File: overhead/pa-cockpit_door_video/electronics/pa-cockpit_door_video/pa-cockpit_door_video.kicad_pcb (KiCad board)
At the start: 2 copper layers, 145 x 47.3 mm, 30 parts, among them J1 Conn_02x01, J3 Conn_02x03_Counter_Clockwise

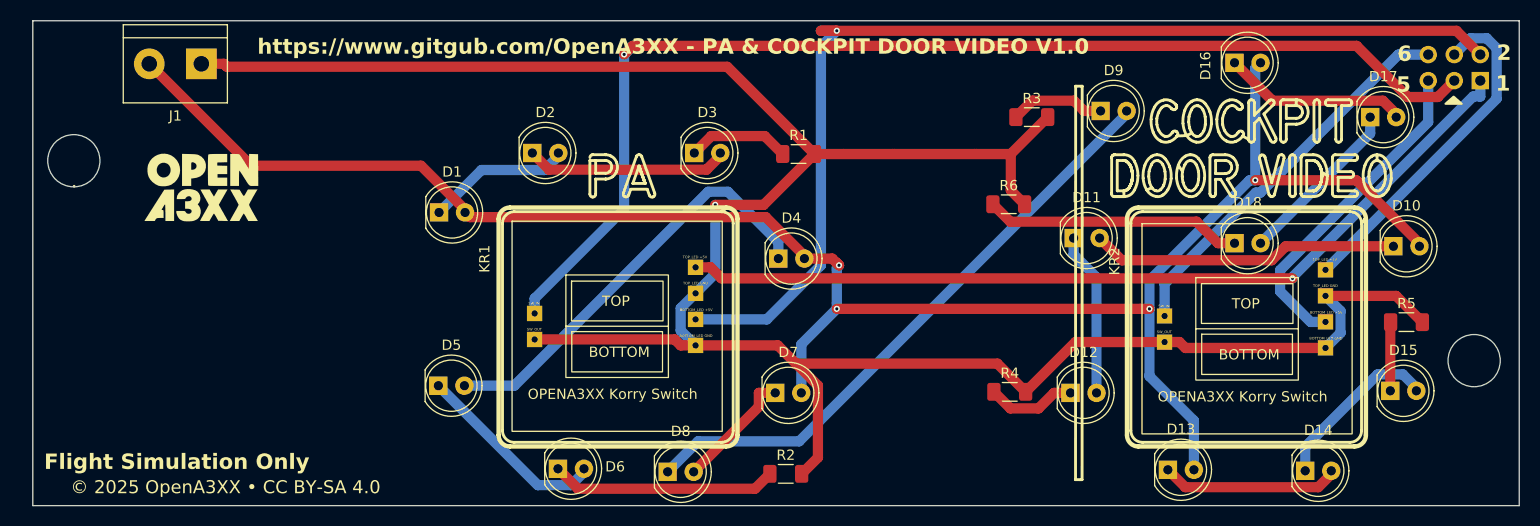
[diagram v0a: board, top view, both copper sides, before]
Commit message: Updated all LEDs for SMD!
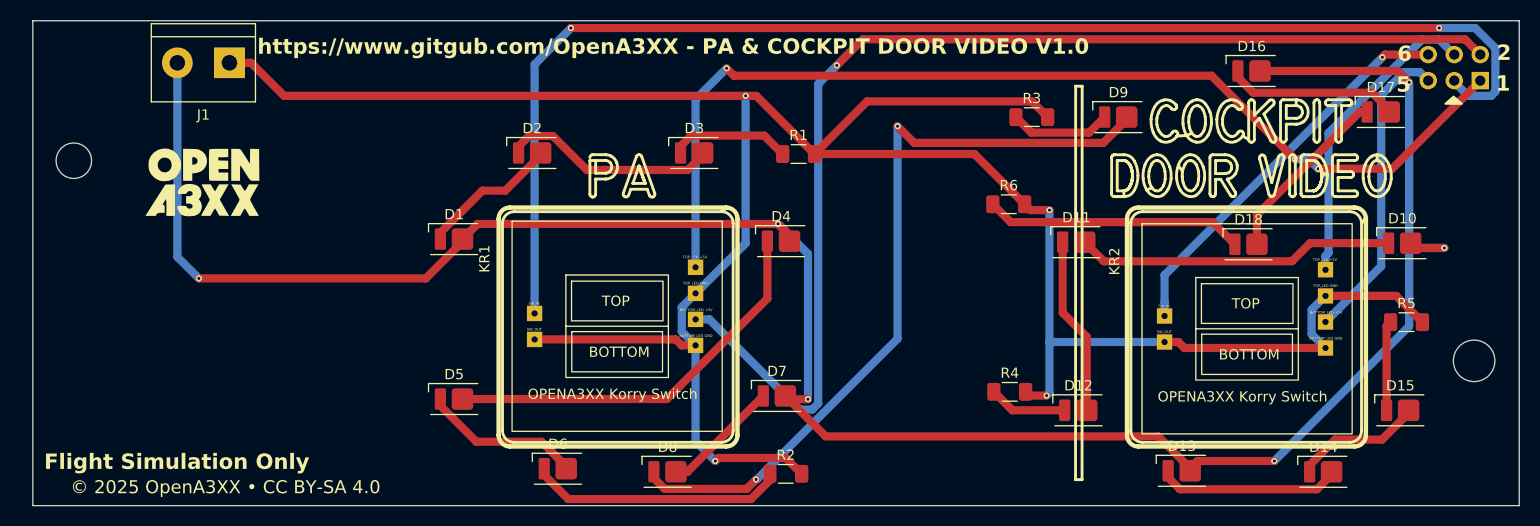
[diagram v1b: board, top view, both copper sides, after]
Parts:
- D1, D10, D11, D12, D13, D14, D15, D16, D17, D18, D2, D3, D4, D5, D6, D7, D8, D9: footprint LED_THT:LED_D5.0mm_Clear -> OpenA3XX:LED_Everlight-SMD3528_3.5x2.8mm_67-21ST
- moved D1 2.99 mm to (111.6, 91.6)
- moved J1 2.74 mm to (89.7, 74.4)
- moved D15 2.14 mm to (203.9, 108.3)
- moved D5 2.02 mm to (111.6, 107.2)
- moved D12 1.87 mm to (172.5, 108.3)
- moved D16 1.86 mm to (189.4, 75.2)
- moved D9 1.84 mm to (176.4, 79.7)
- moved D14 1.77 mm to (196.4, 114.3)
- moved D4 1.72 mm to (143.5, 91.8)
- moved D18 1.38 mm to (189.1, 92.1)
- moved D13 1.37 mm to (182.6, 114.2)
- moved D17 1.15 mm to (202.0, 79.2)
- moved D10 0.92 mm to (204.1, 92.0)
- moved bottom 0.51 mm to (87.3, 86.0)
- moved top 0.51 mm to (87.1, 86.0)
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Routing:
- net +12V: track 186.9 -> 219.0 mm, vias 4 -> 6
- net Net-(D8-K): track 59.5 -> 75.8 mm, vias 0 -> 2
- net Net-(J3-Pin_1): track 86.0 -> 101.8 mm, vias 1 -> 3
- net Net-(J3-Pin_3): track 115.3 -> 129.4 mm, vias 1 -> 2
- net GND: track 231.2 -> 240.4 mm, vias 1 -> 4
- net Net-(J3-Pin_2): track 107.9 -> 114.0 mm
- net Net-(D14-K): track 16.9 -> 12.7 mm
- net Net-(J3-Pin_4): track 33.7 -> 30.1 mm
- net Net-(D5-K): track 19.1 -> 15.6 mm
- net Net-(D6-K): track 22.1 -> 25.0 mm
- net Net-(D4-K): track 42.1 -> 39.4 mm
- net Net-(D15-K): track 6.71 -> 8.76 mm
- net Net-(J3-Pin_5): track 32.2 -> 30.2 mm
- net Net-(D3-K): track 10.0 -> 11.8 mm
- net Net-(D11-K): track 16.0 -> 17.4 mm
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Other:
- outline, holes or cut-outs redrawn

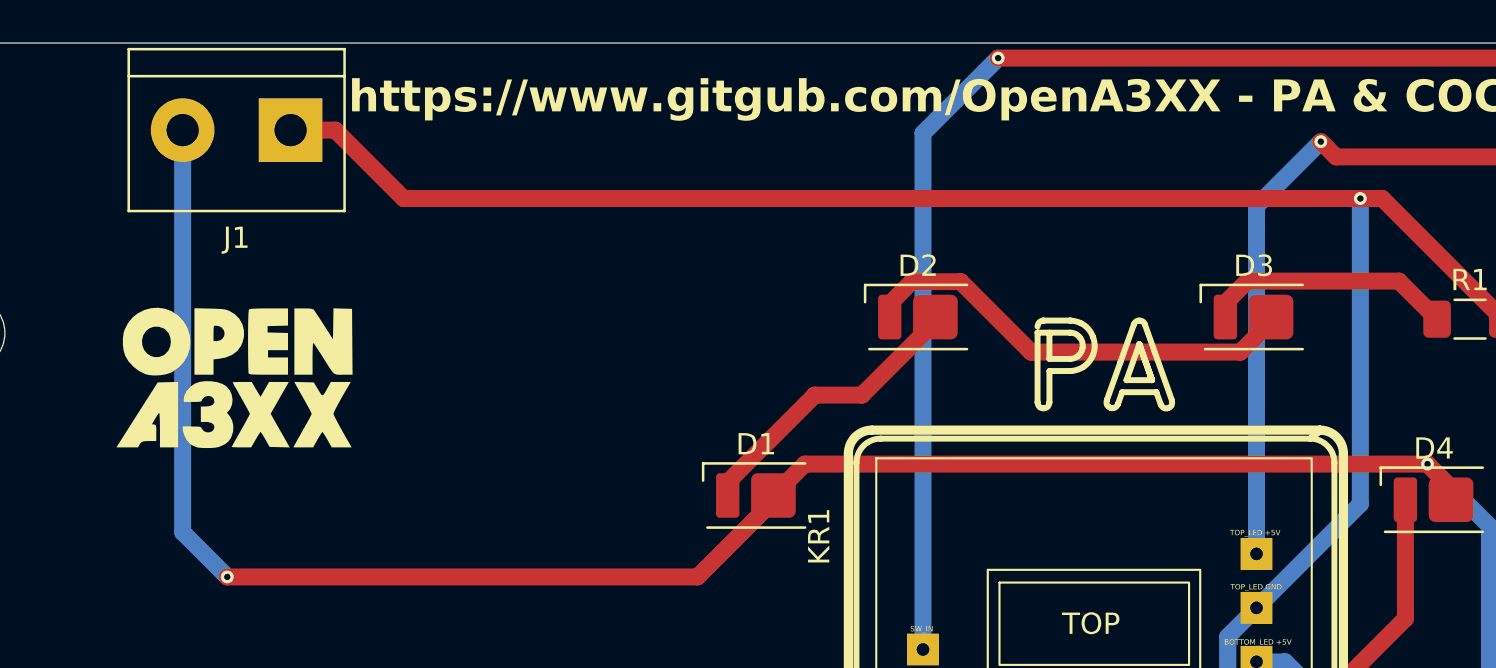
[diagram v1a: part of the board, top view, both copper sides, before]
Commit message: Added terminal connector to 3D models
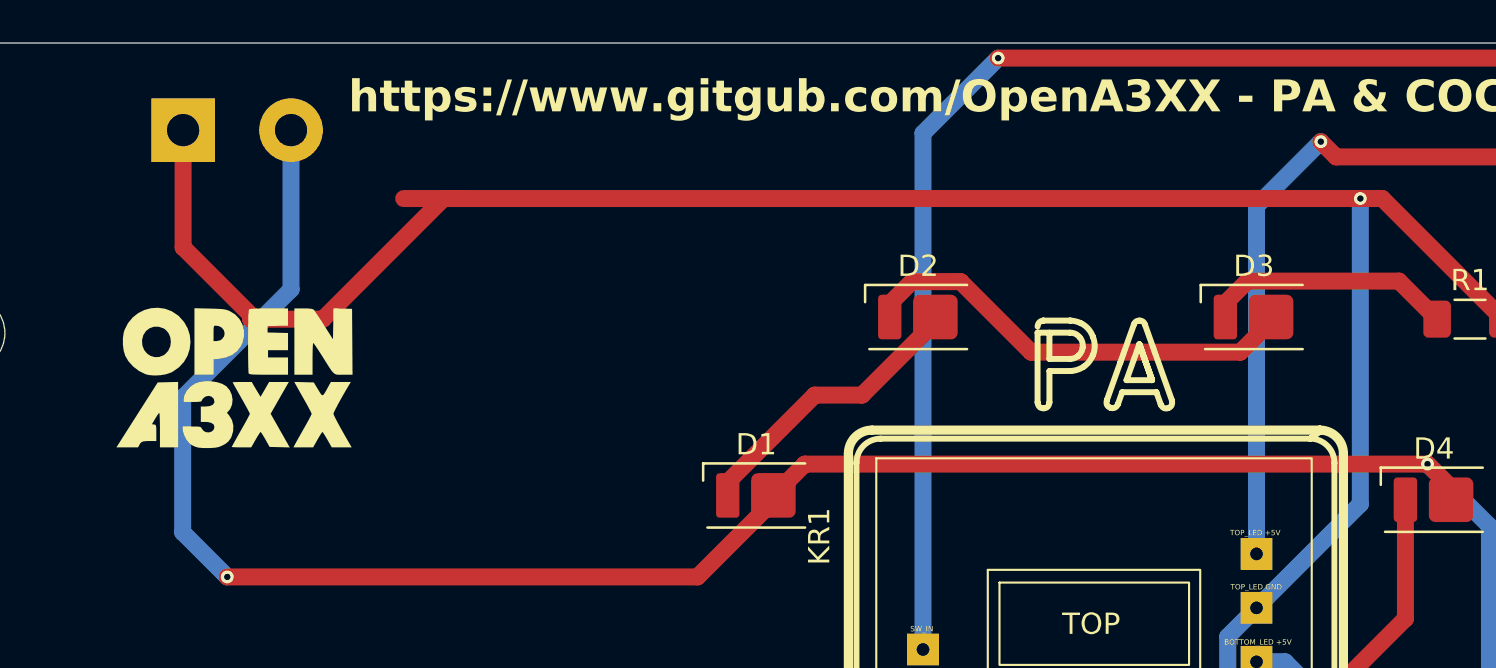
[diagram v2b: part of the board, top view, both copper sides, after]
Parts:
- J1: moved to B.Cu
- moved J1 5.06 mm to (84.6, 74.4), turned to 0 degrees
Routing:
- net GND: track 240.4 -> 256.5 mm
- net +12V: track 219.0 -> 221.1 mm
